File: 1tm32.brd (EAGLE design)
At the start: 63.5 x 63.5 mm, 38 parts, among them IC1 STM32L412RBT6P, IC2 BGM240PA32VNN3, J1 FTSH-107-01-L-DV-K-A, J2 10118192-0001LF, SW1 LL3301FF065QJ, U2 LD39050PU33R, Y1 8MHz, Y2 32.7KHz

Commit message: layout completed
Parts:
- removed J1: FTSH-107-01-L-DV-K-A, ce-capstone:FTSH10701LDVKA
- removed JP1: (no value), pinhead:1X14
- removed R11: 220, ce-capstone:RESC1005X35N
- removed R14: 10k, ce-capstone:RESC1005X40N
- removed R5: 1K, ce-capstone:RESC1005X40N
- added J3: FTSH-105-01-L-D, FTSH-105-01-L-D(bt_connect):SAMTEC_FTSH-105-01-L-D
- added J4: 20021321-00020C4LF, 20021321-00020C4LF(20head):2002132100020C4LF
- added JP2: (no value), pinhead:2X05
- added JP3: (no value), pinhead:2X04
- added JP4: (no value), pinhead:2X03
- added R10: 10K, RC0805JR-0710KL:RESC2012X60N
- added R4: 220, RC0805FR-10220RL:RESC2012X60N
- added R6, R7, R8, R9: 1K, RC0805FR-131KL:RESC2012X60N
- added U$3: LED_R, ce-capstone:LED_SML-P11UTT86R
- R1, R2, R3: device ce-capstone:RESC1005X40N -> RC0805FR-131KL:RESC2012X60N
- moved C39 159.7 mm to (19.3, 32.6)
- moved C2 156.9 mm to (15.3, 27.2), turned to 180 degrees
- moved C4 156.5 mm to (35.2, 7.46), turned to 180 degrees
- moved C37 150.9 mm to (15.3, 32.4), turned to 180 degrees
- moved C40 146.4 mm to (11.6, 19.4), turned to 90 degrees
- moved C3 138.5 mm to (8.23, 8.78), turned to 270 degrees
- moved C34 132.6 mm to (16.4, 19.4), turned to 90 degrees
- moved C35 128.2 mm to (5.04, 19.7), turned to 180 degrees
- moved C30 126.5 mm to (32.6, 27.5), turned to 270 degrees
- moved C33 126.0 mm to (14.0, 19.4), turned to 90 degrees
- moved C31 119.4 mm to (29.7, 14.4), turned to 180 degrees
- moved C32 119.3 mm to (19.7, 14.4), turned to 180 degrees
- moved C28 119.2 mm to (31.5, 31.0)
- moved C29 118.8 mm to (19.9, 30.4)
- moved C27 100.8 mm to (37.3, 13.1)
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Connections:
- removed net LED_G: JP1.10
- removed net PB13: IC1.34
- removed net PB14: IC1.35
- removed net PC0: IC1.8
- removed net PC1: IC1.9
- new net BT_RST: IC1.41, IC2.31, J3.03
- new net N$2: R1.1, U$3.A
- new net PTI_DATA: IC2.27, J3.10
- new net PTI_SYNC: IC2.28, J3.09
- net 3V3: now also J3.01, J4.1, J4.19, J4.2, JP2.4, R10.2, R6.2, R8.2, R9.2; no longer JP1.4, R14.2, R2.2, R3.2, R5.2
- net 5V: now also JP2.9, JP3.1, R2.1, R3.1; no longer J1.3, JP1.3
- net 5V_IN: now also JP2.10; no longer JP1.2
- net ADC1_IN9: now also JP3.8, R3.2
- net ADC2_IN8: now also JP3.6, R2.2
- net BOOT0: now also JP2.7, R7.1; no longer JP1.6, R1.1
- net DBG_SWCLK: now also J3.08
- net DBG_SWDIO: now also J3.07
- net DBG_SWO: now also J3.06
- net GND: now also J3.02, J4.10, J4.12, J4.14, J4.16, J4.18, J4.20, J4.4, J4.6, J4.8, JP2.6, JP2.8, JP3.3, JP3.5, JP3.7, R7.2, U$3.C; no longer J1.11, J1.5, J1.7, JP1.1, JP1.13, JP1.14, R1.2
- net I2C1_SCL: now also JP3.4, R9.1; no longer JP1.8, R3.1
- net I2C1_SDA: now also JP3.2, R8.1; no longer JP1.7, R2.1
- net LED_R: now also IC1.33, JP2.2, R1.2; no longer JP1.9
- net N$3: now also R4.2; no longer R11.1
- net N$5: now also R6.1; no longer R5.1
- net NRST: now also J4.15, JP2.5, R10.1; no longer IC2.31, J1.12, JP1.5, R14.1
- net PH1-OSC-OUT: now also R4.1; no longer R11.2
- net QUADSPI_BK1_IO0: now also JP4.4
- net QUADSPI_BK1_IO1: now also JP4.3
- net QUADSPI_BK1_IO2: now also JP4.2
- net QUADSPI_BK1_IO3: now also JP4.1
- net QUADSPI_BK1_NCS: now also JP4.6
- net QUADSPI_CLK: now also JP4.5
- net SWCLK: now also J4.9; no longer J1.6, J1.9
- net SWDIO: now also J4.7; no longer J1.4
- net SWO: now also J4.13; no longer J1.8
- net USART1_RX: now also J3.05; no longer J1.13, JP1.11
- net USART1_TX: now also J3.04; no longer J1.14, JP1.12
- net USART3_RX: now also JP2.3
- net USART3_TX: now also JP2.1
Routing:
- net GND: track 23.5 -> 137.2 mm, vias 7 -> 21
- net 3V3: track 5.65 -> 61.3 mm, vias 4 -> 14
- net SWDIO: track 73.2 -> 22.1 mm
- net USART1_TX: track 85.0 -> 38.5 mm, vias 2 -> 4
- net 5V: track 44.5 -> 90.7 mm, vias 2 -> 4
- net SWO: track 67.5 -> 22.5 mm
- net SWCLK: track 68.3 -> 23.6 mm
- net BT_RST: track 0.00 -> 39.2 mm, vias 0 -> 3
- net USART1_RX: track 83.4 -> 44.8 mm
- net DBG_SWDIO: track 0.00 -> 29.6 mm, vias 0 -> 2
- net USART3_RX: track 0.00 -> 29.5 mm, vias 0 -> 2
- net DBG_SWCLK: track 0.00 -> 28.9 mm, vias 0 -> 2
- net DBG_SWO: track 0.00 -> 26.5 mm, vias 0 -> 2
- net USART3_TX: track 0.00 -> 26.1 mm, vias 0 -> 2
- net ADC1_IN9: track 0.00 -> 23.9 mm, vias 0 -> 2
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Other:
- board size 63.5 x 63.5 mm -> 50.8 x 50.8 mm
- board text added: "cUWUb3D"
- board text removed: "cUWUbe"

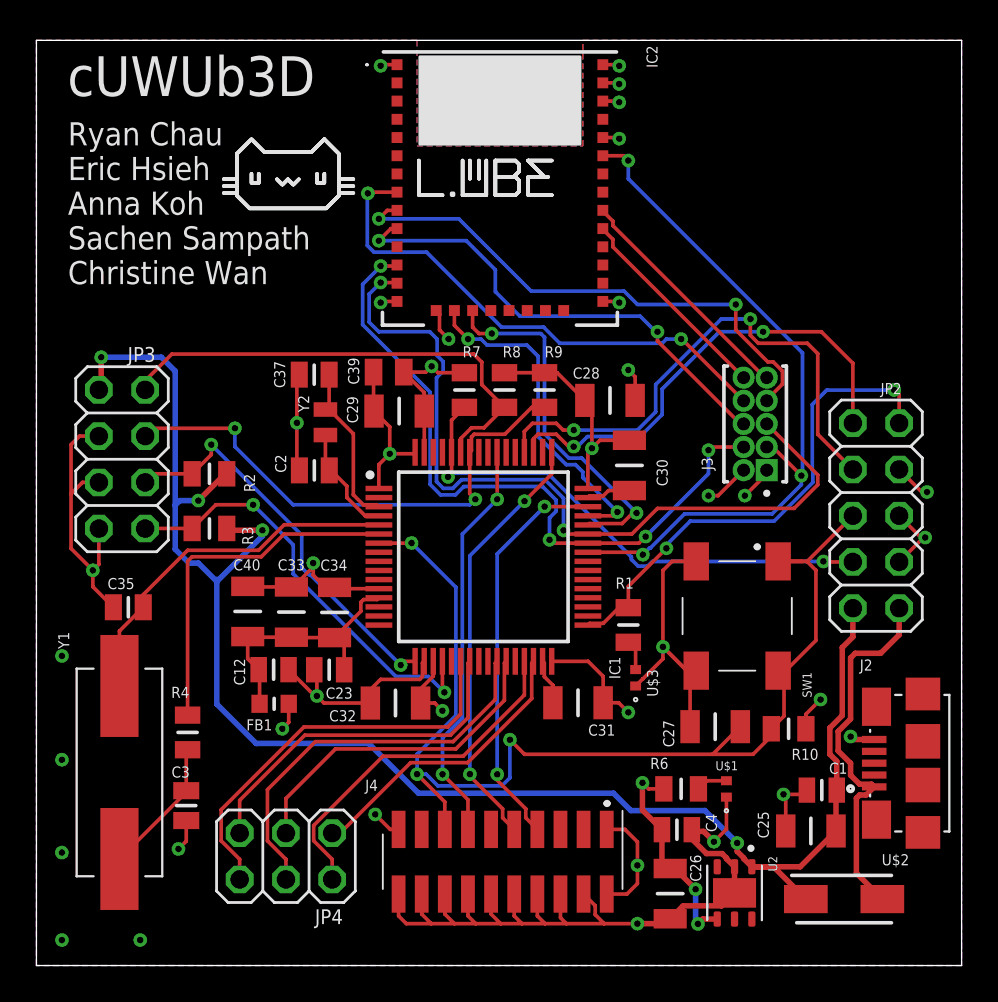
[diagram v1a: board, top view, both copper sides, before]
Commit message: add gnd vias and change adc resistors
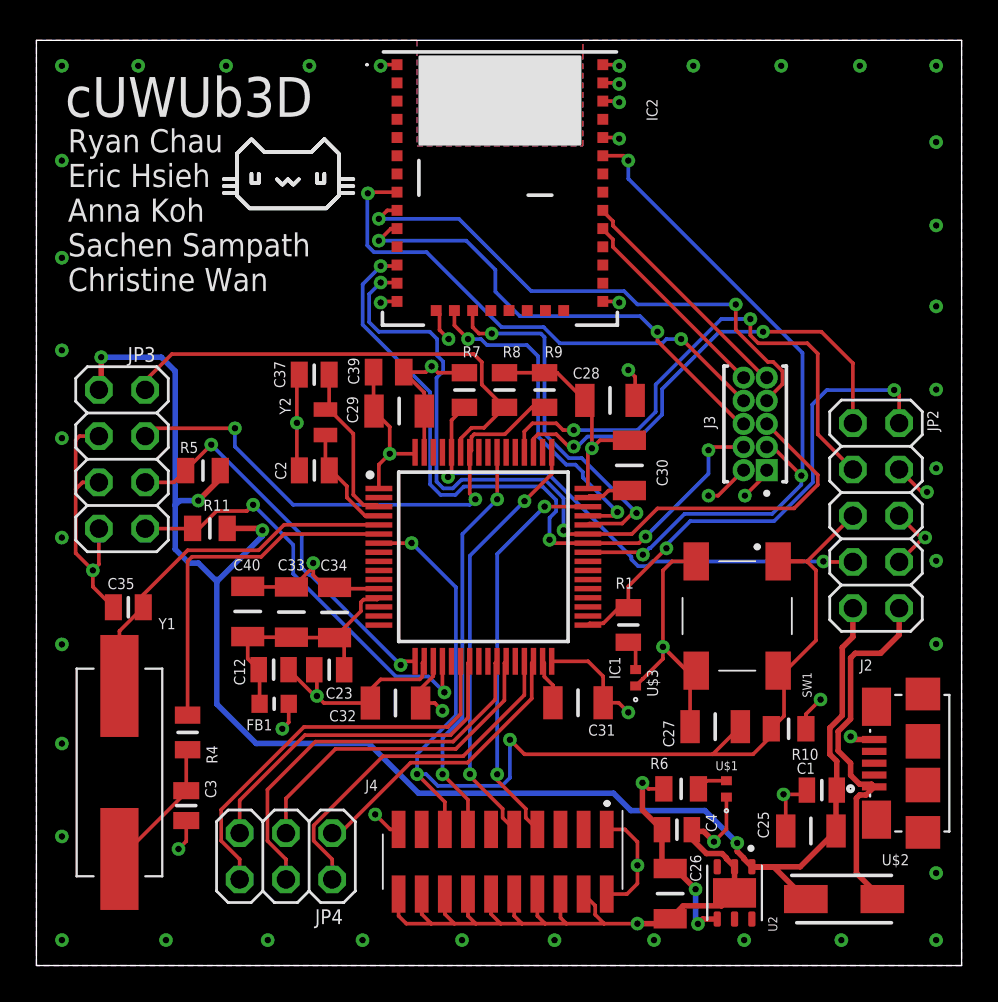
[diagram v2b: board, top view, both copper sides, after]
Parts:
- removed R2, R3: 1K, RC0805FR-131KL:RESC2012X60N
- added R11, R5: 10K, RC0805JR-0710KL:RESC2012X60N
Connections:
- net 5V: now also R11.1, R5.1; no longer R2.1, R3.1
- net ADC1_IN9: now also R11.2; no longer R3.2
- net ADC2_IN8: now also R5.2; no longer R2.2
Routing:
- net GND: track 137.2 -> 136.7 mm, vias 21 -> 55
